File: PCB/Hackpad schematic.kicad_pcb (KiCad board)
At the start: 2 copper layers, 67 x 47 mm, 8 parts, among them SW1 SW_Push, SW2 SW_Push, SW3 SW_Push, SW4 SW_Push, U1 MOUDLE-SEEEDUINO-XIAO

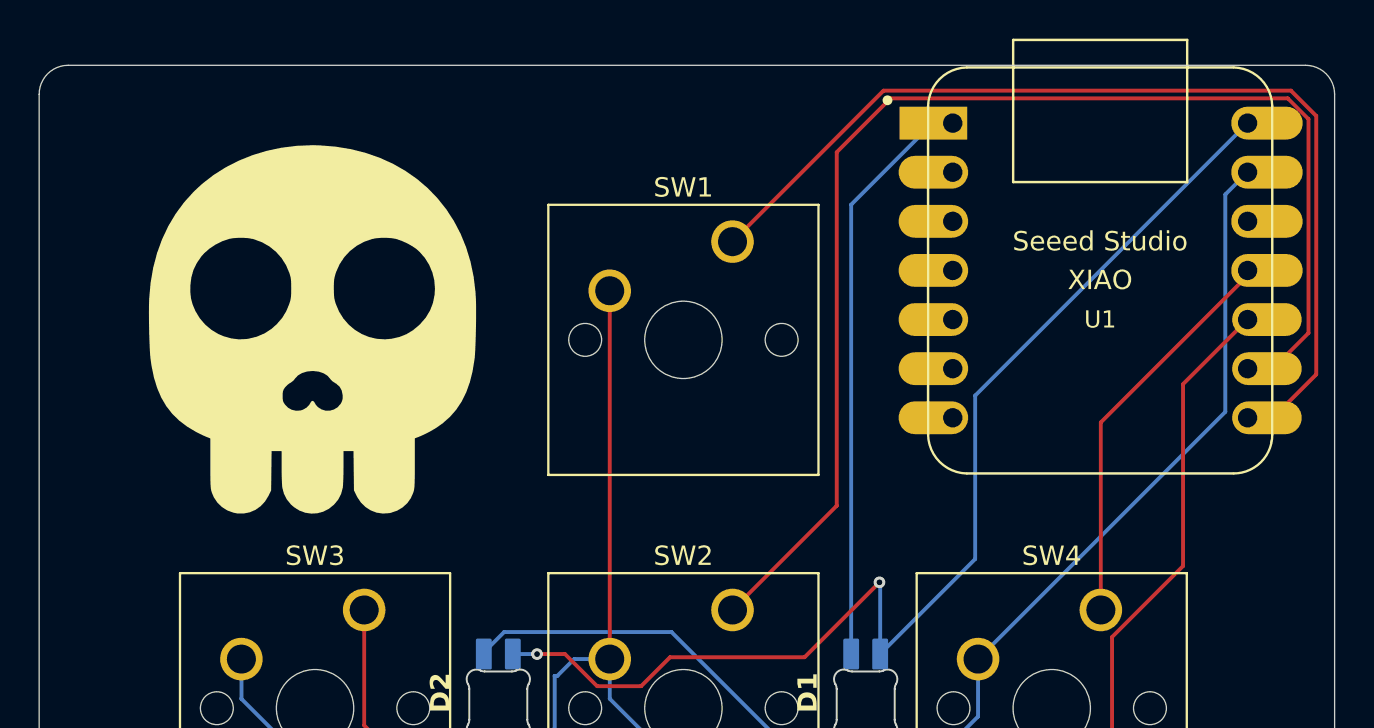
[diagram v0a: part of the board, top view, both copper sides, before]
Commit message: Added rotary knob
Added rotary knob. Made skull smaller
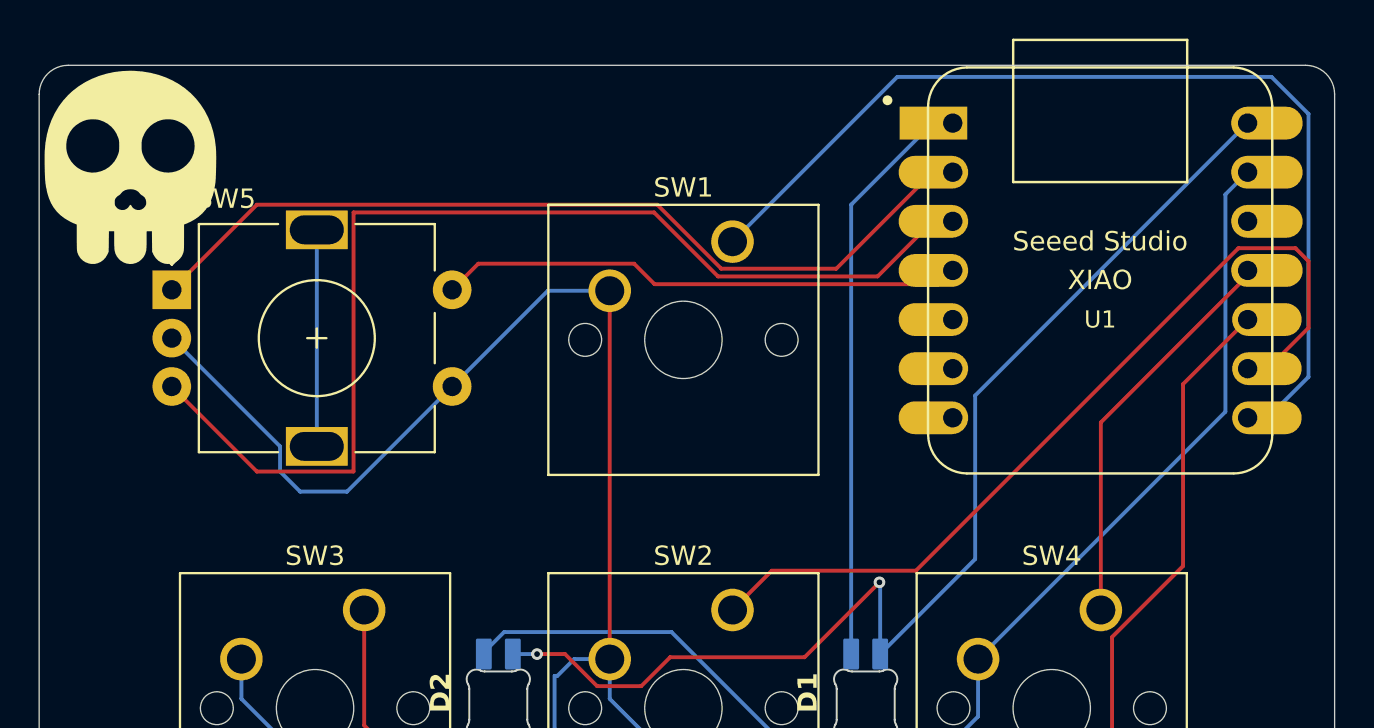
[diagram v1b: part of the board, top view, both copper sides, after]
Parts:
- added SW5: RotaryEncoder_Switch, Rotary_Encoder:RotaryEncoder_Alps_EC11E-Switch_Vertical_H20mm, F.Cu at (121.2, 78.9)
- moved G*** 12.6 mm to (119.0, 72.6)
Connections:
- U1 pad 2: unconnected-(U1-PA4_A1_D1-Pad2) -> Net-(U1-PA4_A1_D1)
- U1 pad 3: unconnected-(U1-PA10_A2_D2-Pad3) -> Net-(U1-PA10_A2_D2)
- U1 pad 4: unconnected-(U1-PA11_A3_D3-Pad4) -> Net-(U1-PA11_A3_D3)
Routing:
- net Net-(U1-PA10_A2_D2): track 0.00 -> 58.2 mm
- net Net-(U1-PA4_A1_D1): track 0.00 -> 45.7 mm, vias 0 -> 1
- net GND: track 104.3 -> 135.3 mm
- net Net-(U1-PA11_A3_D3): track 0.00 -> 27.2 mm
- net Net-(U1-PA7_A8_D8_SCK): track 67.9 -> 46.3 mm
- net (no net): track 0.00 -> 11.2 mm
- net Net-(U1-PB09_A7_D7_RX): track 51.9 -> 52.8 mm

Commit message: Add rotary encoder (SW6) and reorganize PCB layout
Added a new Alps EC11E rotary encoder (SW6) to the PCB at position (1.525, 4.625). Repositioned existing rotary encoder (SW5) and the logo footprint. Updated PCB traces and routing to accommodate the new component. Updated documentation images and added a skull emoji asset.
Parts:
- added SW6: RotaryEncoder_Switch, Rotary_Encoder:RotaryEncoder_Alps_EC11E-Switch_Vertical_H20mm, F.Cu at (1.52, 4.62)
- moved G*** 68.0 mm to (176.4, 109.1)
- moved SW5 4.96 mm to (117.7, 75.4)
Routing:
- net (no net): track 11.2 -> 0.00 mm
- net Net-(U1-PA10_A2_D2): track 58.2 -> 49.4 mm
- net Net-(U1-PA11_A3_D3): track 27.2 -> 31.0 mm
- net GND: track 135.3 -> 132.1 mm
- net Net-(U1-PA4_A1_D1): track 45.7 -> 48.6 mm

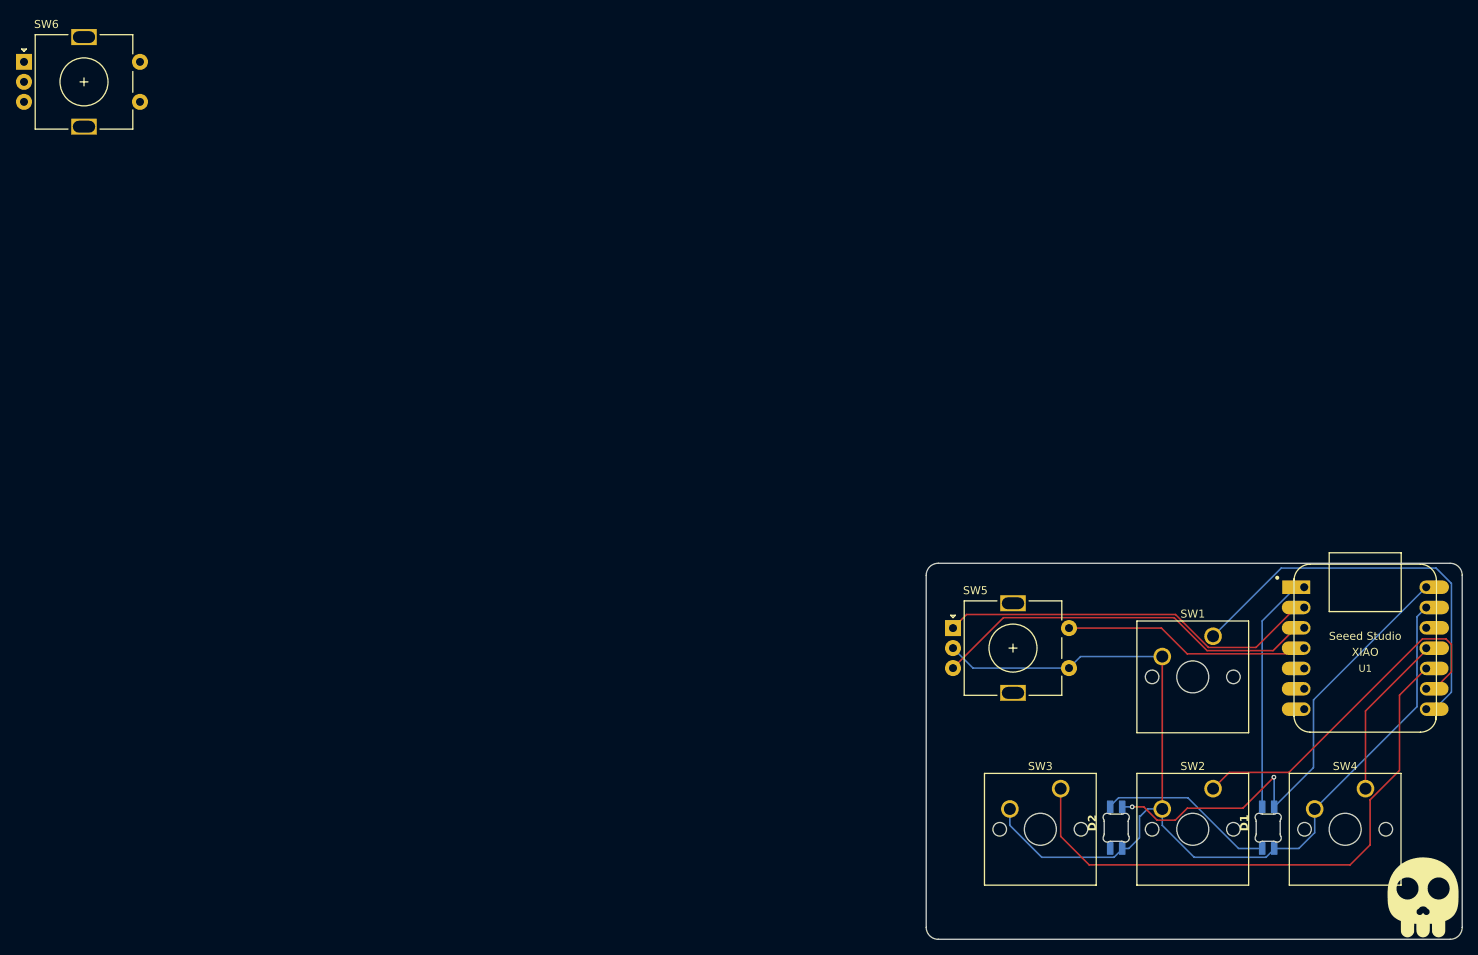
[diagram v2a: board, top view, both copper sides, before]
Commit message: Flipped microcontroller
Flipped microcontroller. Updated images and 3d model. Added KMK library
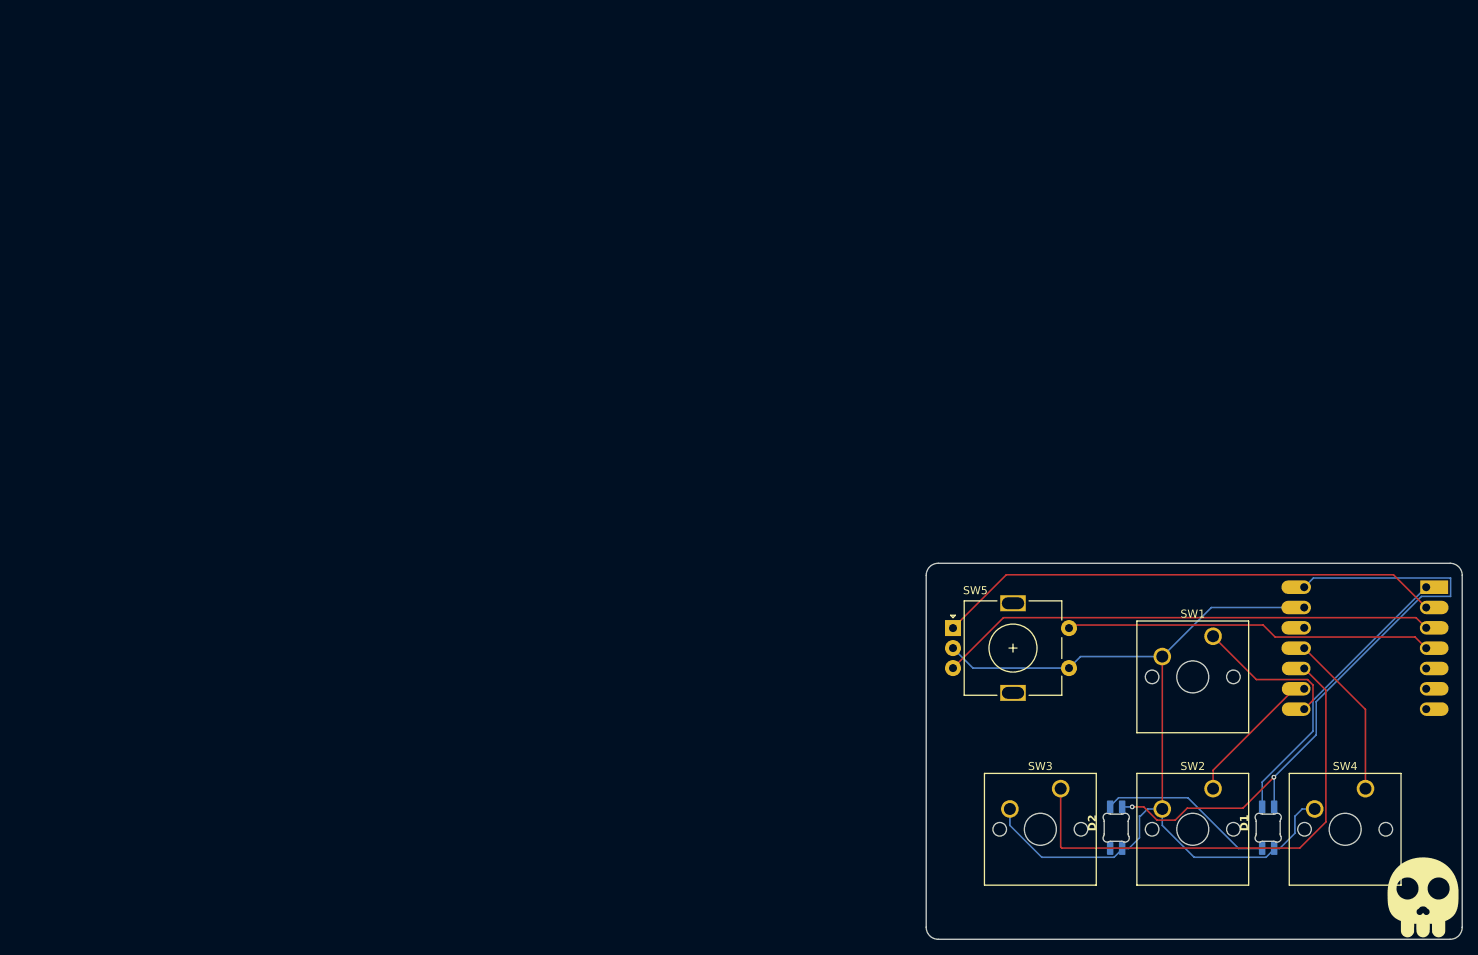
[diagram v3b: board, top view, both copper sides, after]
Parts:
- removed SW6: RotaryEncoder_Switch, Rotary_Encoder:RotaryEncoder_Alps_EC11E-Switch_Vertical_H20mm
- U1: moved to B.Cu
- turned U1 to 180 degrees
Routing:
- net Net-(U1-PB09_A7_D7_RX): track 52.8 -> 18.5 mm
- net Net-(U1-PA7_A8_D8_SCK): track 46.3 -> 17.9 mm
- net VCC: track 60.9 -> 80.6 mm
- net Net-(U1-PA4_A1_D1): track 48.6 -> 63.6 mm, vias 1 -> 0
- net Net-(U1-PA11_A3_D3): track 31.0 -> 46.0 mm
- net Net-(U1-PA10_A2_D2): track 49.4 -> 62.3 mm
- net GND: track 132.1 -> 122.0 mm, vias 0 -> 1
- net Net-(U1-PA5_A9_D9_MISO): track 72.1 -> 62.2 mm
- net RGB_Lighting: track 30.2 -> 36.0 mm
- net unconnected-(U1-PA9_A5_D5_SCL-Pad6): track 0.00 -> 2.07 mm
- net unconnected-(U1-3V3-Pad12): track 0.00 -> 1.04 mm
- net unconnected-(U1-PB08_A6_D6_TX-Pad7): track 0.00 -> 1.04 mm
